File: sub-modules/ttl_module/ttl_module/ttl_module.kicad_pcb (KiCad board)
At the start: 2 copper layers, 50 x 19.4 mm, 1 part, among them J1 Conn_02x06_Odd_Even

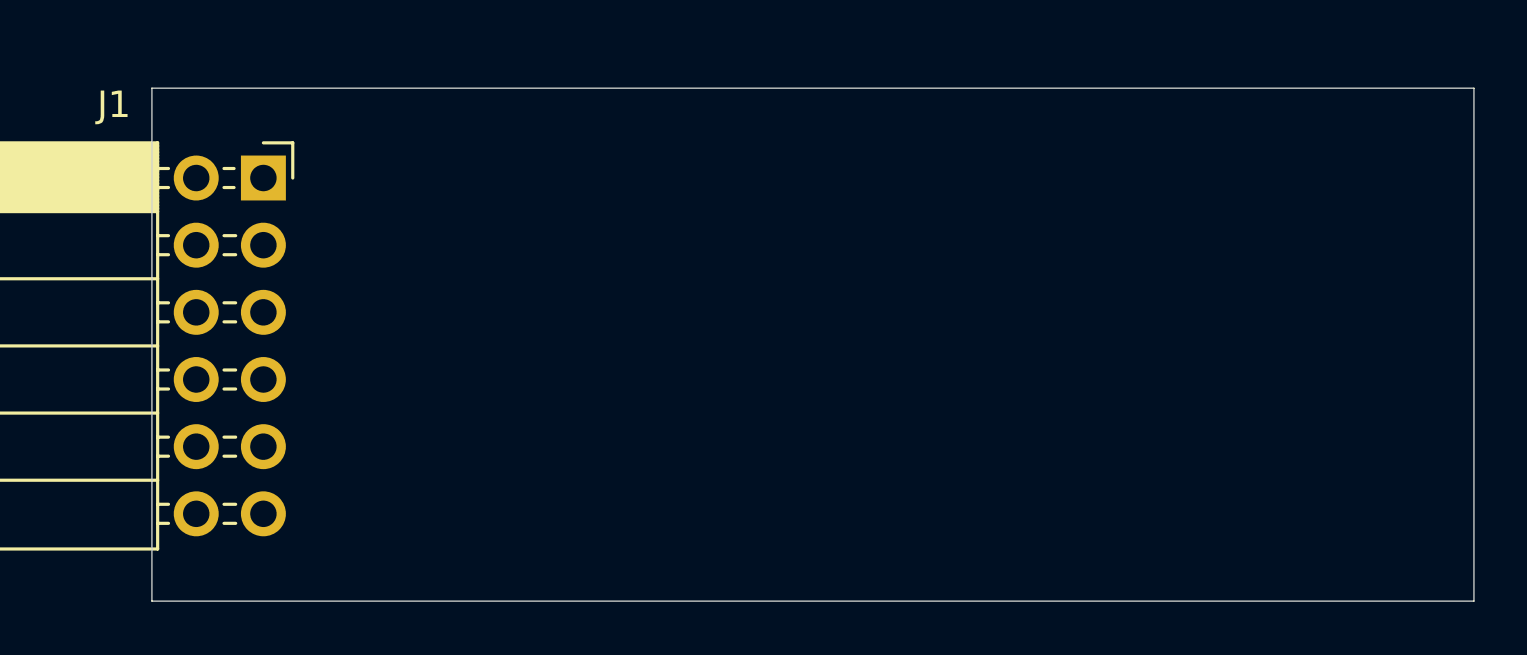
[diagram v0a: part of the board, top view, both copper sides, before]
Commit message: Updated Schematic and PCB for first pass at the design
Signed-off-by: Marc Kelly <mpkelly@achenar.co.uk>
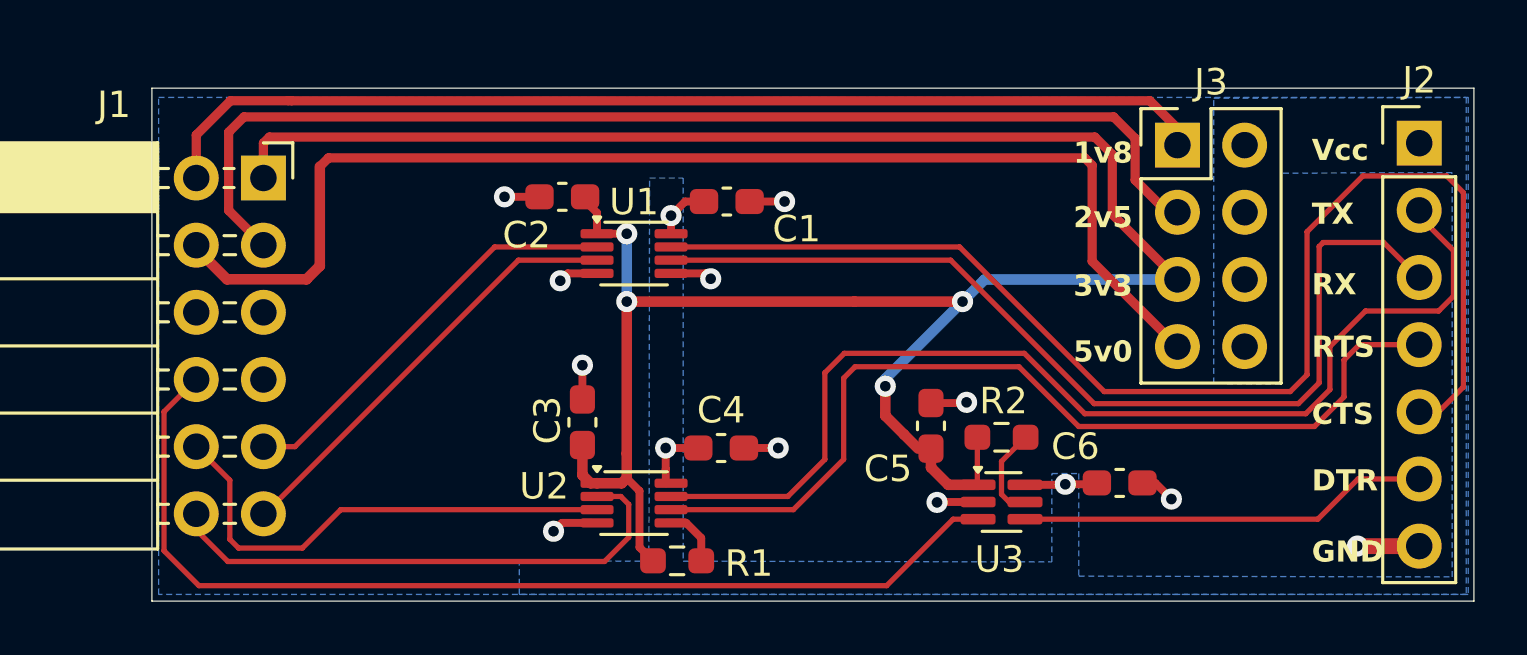
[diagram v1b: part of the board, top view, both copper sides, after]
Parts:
- added C1: 100n, Capacitor_SMD:C_0603_1608Metric_Pad1.08x0.95mm_HandSolder, F.Cu at (72.5, 61.1)
- added C2: 100n, Capacitor_SMD:C_0603_1608Metric_Pad1.08x0.95mm_HandSolder, F.Cu at (66.3, 60.9)
- added C3: 100n, Capacitor_SMD:C_0603_1608Metric_Pad1.08x0.95mm_HandSolder, F.Cu at (67.1, 69.4)
- added C4: 100n, Capacitor_SMD:C_0603_1608Metric_Pad1.08x0.95mm_HandSolder, F.Cu at (72.3, 70.4)
- added C5: 100n, Capacitor_SMD:C_0603_1608Metric_Pad1.08x0.95mm_HandSolder, F.Cu at (80.3, 69.6)
- added C6: 100n, Capacitor_SMD:C_0603_1608Metric_Pad1.08x0.95mm_HandSolder, F.Cu at (87.4, 71.7)
- added J2: Output, Connector_PinHeader_2.54mm:PinHeader_1x07_P2.54mm_Vertical, F.Cu at (98.7, 58.9)
- added J3: VCC Selection, Connector_PinHeader_2.54mm:PinHeader_2x04_P2.54mm_Vertical, F.Cu at (89.6, 59.0)
- added R1: 4.7k, Resistor_SMD:R_0603_1608Metric_Pad0.98x0.95mm_HandSolder, F.Cu at (70.7, 74.7)
- added R2: 4.7k, Resistor_SMD:R_0603_1608Metric_Pad0.98x0.95mm_HandSolder, F.Cu at (82.9, 70.0)
- added U1: SN74LVC2T45DCUR, Package_SO:VSSOP-8_2.3x2mm_P0.5mm, F.Cu at (69.0, 63.1)
- added U2: SN74LVC2T45DCUR, Package_SO:VSSOP-8_2.3x2mm_P0.5mm, F.Cu at (69.0, 72.5)
- added U3: SN74LVC1T45DCK, Package_TO_SOT_SMD:SOT-363_SC-70-6, F.Cu at (82.9, 72.5)
- J1: value Conn_02x06_Odd_Even -> Input
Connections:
- net /GND renamed GND
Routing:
- net /3v3: track 0.00 -> 91.4 mm, vias 0 -> 4
- net /CTS_IN: track 0.00 -> 48.4 mm
- net /VBUS: track 0.00 -> 47.2 mm
- net /2v5: track 0.00 -> 43.4 mm
- net /TX_OUT: track 0.00 -> 41.3 mm
- net /1v8: track 0.00 -> 40.3 mm
- net /DTR: track 0.00 -> 39.4 mm
- net /RX_IN: track 0.00 -> 36.6 mm
- net /RTS_OUT: track 0.00 -> 35.9 mm
- net /TX: track 0.00 -> 20.6 mm
- net /RTS: track 0.00 -> 18.5 mm
- net /RX: track 0.00 -> 17.3 mm
- net GND: track 0.00 -> 16.5 mm, vias 0 -> 11
- net /CTS: track 0.00 -> 15.7 mm
- net /DTR_OUT: track 0.00 -> 15.5 mm
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- added copper zone on B.Cu, net GND
- added copper zone on B.Cu, net VCC
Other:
- board text added: "1v8"
- board text added: "2v5"
- board text added: "3v3"
- board text added: "5v0"
- board text added: "CTS"
- board text added: "DTR"
- board text added: "GND"
- board text added: "RTS"
- board text added: "RX"
- board text added: "TX"
- board text added: "Vcc"

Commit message: Quick update to the ttl module board layout
Signed-off-by: Marc Kelly <mpkelly@achenar.co.uk>
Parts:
- J1: footprint Connector_PinSocket_2.54mm:PinSocket_2x06_P2.54mm_Horizontal -> Local:PinSocket_2x06_P2.54mm_Horizontal
- moved C2 69.3 mm to (134.9, 50.7)
- moved C4 69.3 mm to (140.9, 60.2)
- moved C5 69.3 mm to (148.8, 59.4)
- moved J2 69.3 mm to (167.3, 48.7)
- moved R2 69.3 mm to (151.5, 59.8)
- moved C3 69.3 mm to (135.7, 59.3)
- moved C6 69.3 mm to (156.0, 61.6)
- moved J1 69.3 mm to (123.6, 50.0)
- moved J3 69.3 mm to (158.2, 48.8)
- moved R1 69.3 mm to (139.2, 64.5)
- moved U1 69.3 mm to (137.6, 52.9)
- moved U2 69.3 mm to (137.6, 62.3)
- moved U3 69.3 mm to (151.5, 62.3)
- moved C1 69.3 mm to (141.1, 50.9)
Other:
- board text added: "0"
- board text added: "0 mm"
- board text added: "0.01 mm"
- board text added: "0.02"
- board text added: "0.035 mm"
- board text added: "0.1016 mm / 0.0000 mm"
- board text added: "0.2000 mm"
- board text added: "1"
- board text added: "1.51 mm"
- board text added: "1.6000 mm"
- board text added: "2"
- board text added: "3.3"
- board text added: "4.5"
- board text added: "50.0000 mm x 19.4000 mm"
- board text added: "B.Cu"
- board text added: "B.Mask"
- board text added: "B.Paste"
- board text added: "B.Silkscreen"
- board text added: "BOARD CHARACTERISTICS"
- board text added: "Board Thickness:"
- board text added: "Board overall dimensions:"
- board text added: "Bottom Silk Screen"
- board text added: "Bottom Solder Mask"
- board text added: "Bottom Solder Paste"
- board text added: "Castellated pads:"
- board text added: "Color"
- board text added: "Copper Finish:"
- board text added: "Copper Layer Count:"
- board text added: "Dielectric"
- board text added: "Edge card connectors:"
- board text added: "Epsilon R"
- board text added: "F.Cu"
- board text added: "F.Mask"
- board text added: "F.Paste"
- board text added: "F.Silkscreen"
- board text added: "FR4"
- board text added: "HAL lead-free"
- board text added: "Impedance Control:"
- board text added: "Layer Name"
- board text added: "Loss Tangent"
- board text added: "Material"
- board text added: "Min hole diameter:"
- board text added: "Min track/spacing:"
- board text added: "No"
- board text added: "Not specified"
- board text added: "Plated Board Edge:"
- board text added: "Thickness (mm)"
- board text added: "Top Silk Screen"
- board text added: "Top Solder Mask"
- board text added: "Top Solder Paste"
- board text added: "Type"
- board text added: "copper"
- board text added: "core"

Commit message: Update schematics after moving to KiCad 10
Added some footprints to a local lib, as the silkscreen caused issues.

Signed-off-by: Marc Kelly <mpkelly@achenar.co.uk>
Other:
- board text added: "(c) Achenarian Empire"
- board text added: "Imperial TTL->TTL"

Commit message: Sorting out BOMs
Signed-off-by: Marc Kelly <mpkelly@achenar.co.uk>
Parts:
- U1, U2: value SN74LVC2T45DCUR -> SN74LVC2T45DCDTR; footprint Package_SO:VSSOP-8_2.3x2mm_P0.5mm -> Snapeda:SOP65P400X130-8N
- moved R1 3.10 mm to (142.2, 63.6), turned to 0 degrees
- moved C1 1.25 mm to (142.1, 51.7)
- moved C3 1.05 mm to (134.7, 59.7), turned to 0 degrees
- moved C4 0.55 mm to (141.2, 59.8)
- moved C2 0.41 mm to (134.9, 50.3)
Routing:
- net /3v3: track 91.4 -> 97.2 mm
- net GND: track 16.5 -> 15.4 mm
- net VCC: track 7.61 -> 8.63 mm
